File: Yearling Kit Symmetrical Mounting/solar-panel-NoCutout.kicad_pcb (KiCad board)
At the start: 4 copper layers, 83 x 98 mm, 25 parts, among them J1 CON-5040500591, J2 Conn_01x01, J3 Conn_01x01, J4 Conn_01x01, J5 Conn_01x01, U1 VEML7700, U2 MCP9808_DFN, U3 DRV2605LDGS

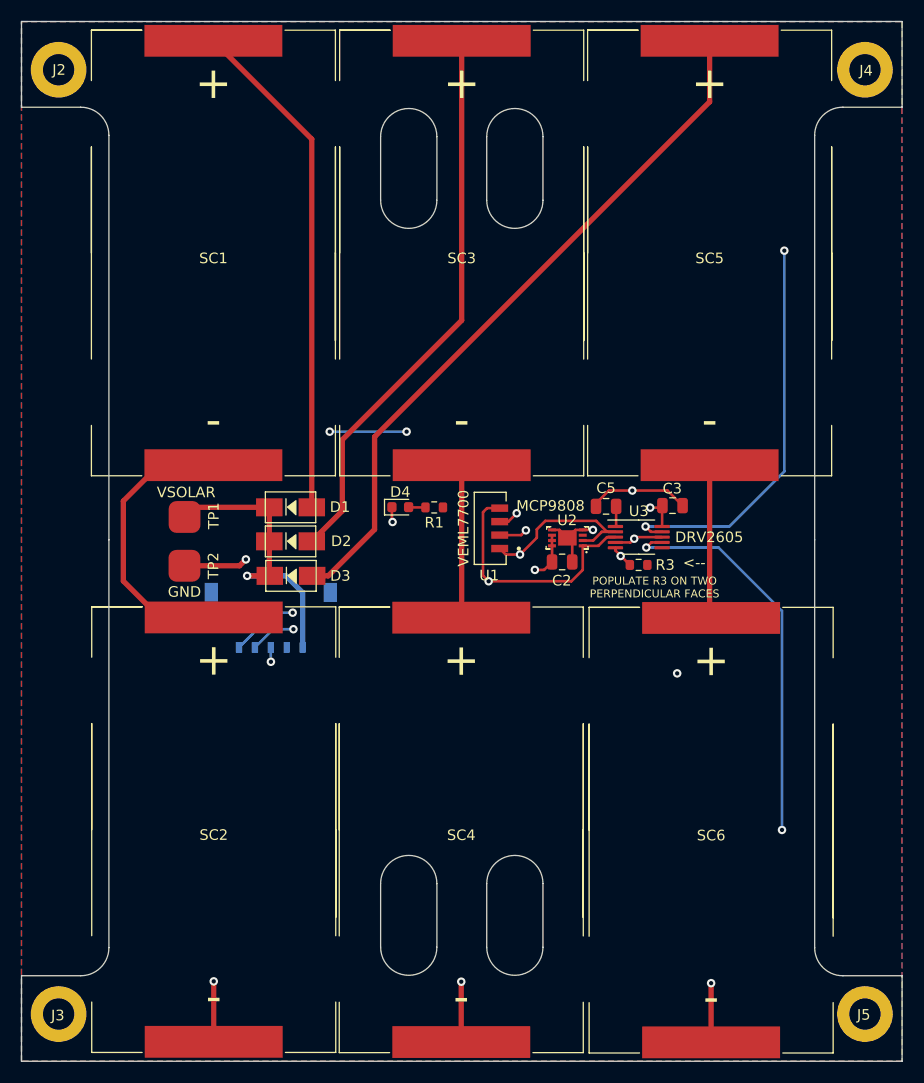
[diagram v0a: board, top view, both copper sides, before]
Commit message: updated no cutout for production
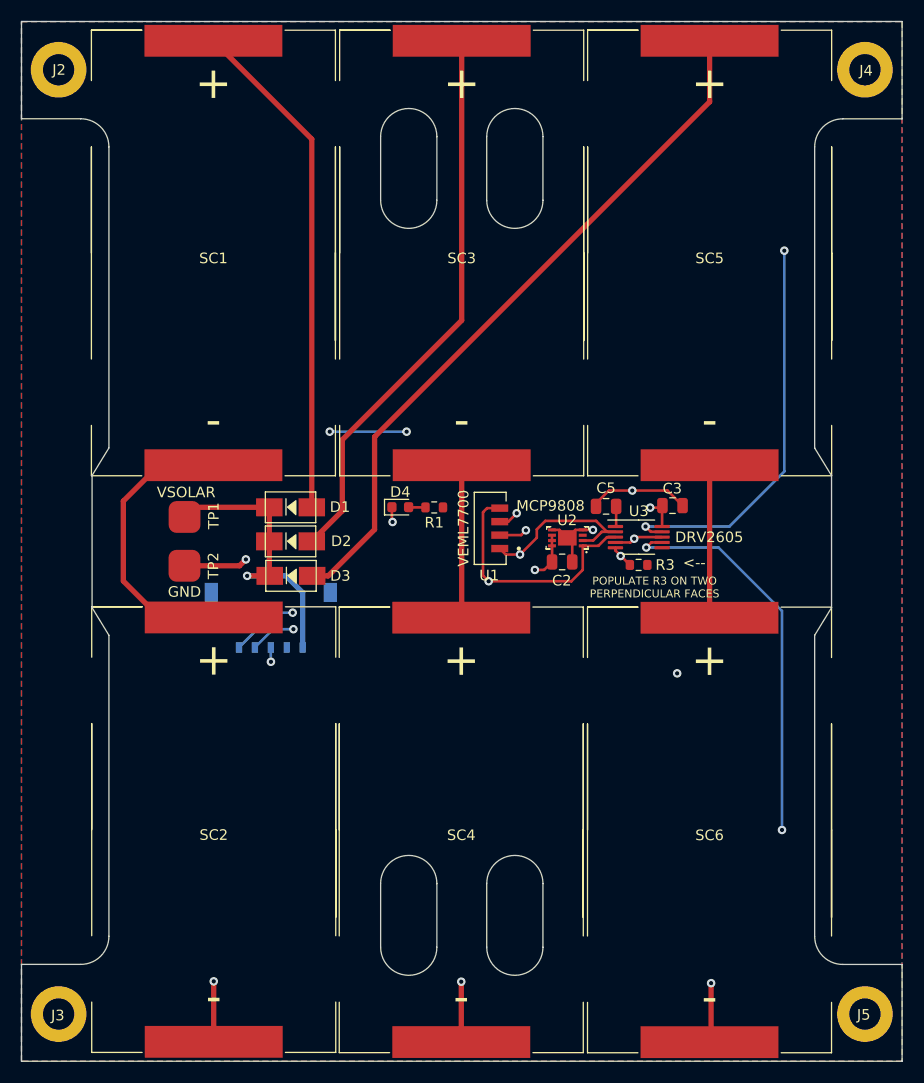
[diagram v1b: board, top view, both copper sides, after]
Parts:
- moved SC6 0.15 mm to (167.8, 141.9)
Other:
- outline, holes or cut-outs redrawn
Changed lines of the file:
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@@
       (rotate (xyz -90 0 0))
+    )
+    (model "C:/Users/bronc/Downloads/solar_cell.step"
+      (offset (xyz -3.4 -0.6 0))
+      (scale (xyz 1 1 1))
+      (rotate (xyz 0 0 0))
     )
   )
@@
       (rotate (xyz -90 0 0))
     )
+    (model "C:/Users/bronc/Downloads/solar_cell.step"
+      (offset (xyz -3.3 -0.6 0))
+      (scale (xyz 1 1 1))
+      (rotate (xyz 0 0 0))
+    )
   )
   (footprint "SolarPanelBoards:KXOB101K08F-TR" (layer "F.Cu")
@@
       (rotate (xyz -90 0 0))
     )
+    (model "C:/Users/bronc/Downloads/solar_cell.step"
+      (offset (xyz -3.3 -0.6 0))
+      (scale (xyz 1 1 1))
+      (rotate (xyz 0 0 0))
+    )
   )
   (footprint "SolarPanelBoards:KXOB101K08F-TR" (layer "F.Cu")
@@
       (rotate (xyz -90 0 0))
     )
+    (model "C:/Users/bronc/Downloads/solar_cell.step"
+      (offset (xyz -3.3 -0.6 0))
+      (scale (xyz 1 1 1))
+      (rotate (xyz 0 0 0))
+    )
   )
   (footprint "SolarPanelBoards:DO-214AC" (layer "F.Cu")
@@
   )
   (footprint "SolarPanelBoards:KXOB101K08F-TR" (layer "F.Cu")
-    (at 168 141.97)
+    (at 167.85 141.95)
     (property "Sheetfile" "solar-panel-NoCutout.kicad_sch")
     (property "Sheetname" "")
@@
       (rotate (xyz -90 0 0))
     )
+    (model "C:/Users/bronc/Downloads/solar_cell.step"
+      (offset (xyz -3.3 -0.6 0))
+      (scale (xyz 1 1 1))
+      (rotate (xyz 0 0 0))
+    )
   )
   (footprint "Capacitor_SMD:C_0805_2012Metric" (layer "F.Cu")
@@
     (pad "4" smd rect locked (at -0.9 1.905 180) (size 1.6 0.7) (layers "F.Cu" "F.Paste" "F.Mask")
       (net 8 "SDA") (pinfunction "SDA") (pintype "bidirectional"))
+    (model "${KIPRJMOD}/Extras/3-DComponents/84592VEML7700.stp"
+      (offset (xyz 0 0 0.3))
+      (scale (xyz 1 1 1))
+      (rotate (xyz 0 0 90))
+    )
   )
   (footprint "Resistor_SMD:R_0603_1608Metric" (layer "F.Cu")
@@
       (scale (xyz 1 1 1))
       (rotate (xyz -90 0 0))
+    )
+    (model "C:/Users/bronc/Downloads/solar_cell.step"
+      (offset (xyz -3.3 -0.6 0))
+      (scale (xyz 1 1 1))
+      (rotate (xyz 0 0 0))
     )
   )
@@
   (gr_line (start 152.15 76.6) (end 152.15 82.6) (layer "Edge.Cuts") (width 0.05))
   (gr_line (start 186 65.75) (end 103 65.75) (layer "Edge.Cuts") (width 0.05))
-  (gr_line (start 108.58 73.83) (end 103 73.83) (layer "Edge.Cuts") (width 0.05))
-  (gr_arc (start 108.58 73.83) (mid 110.461763 74.601155) (end 111.24 76.48) (layer "Edge.Cuts") (width 0.05))
-  (gr_line (start 103 65.75) (end 103 73.83) (layer "Edge.Cuts") (width 0.05))
-  (gr_line (start 103 155.69) (end 103 163.75) (layer "Edge.Cuts") (width 0.05))
+  (gr_line (start 108.58 74.92) (end 103 74.92) (layer "Edge.Cuts") (width 0.05))
+  (gr_arc (start 108.58 74.92) (mid 110.461789 75.69114) (end 111.24 77.57) (layer "Edge.Cuts") (width 0.05))
+  (gr_line (start 103 65.75) (end 103 74.92) (layer "Edge.Cuts") (width 0.05))
+  (gr_line (start 103 154.62) (end 103 163.75) (layer "Edge.Cuts") (width 0.05))
   (gr_arc (start 142.15 82.6) (mid 139.5 85.25) (end 136.85 82.6) (layer "Edge.Cuts") (width 0.05))
-  (gr_line (start 186 73.83) (end 180.42 73.83) (layer "Edge.Cuts") (width 0.05))
-  (gr_line (start 177.76 76.48) (end 177.76 114.6) (layer "Edge.Cuts") (width 0.05))
+  (gr_line (start 186 74.925) (end 180.42 74.925) (layer "Edge.Cuts") (width 0.05))
   (gr_arc (start 146.85 76.6) (mid 149.5 73.95) (end 152.15 76.6) (layer "Edge.Cuts") (width 0.05))
-  (gr_line (start 186 73.83) (end 186 65.75) (layer "Edge.Cuts") (width 0.05))
+  (gr_line (start 186 74.925) (end 186 65.75) (layer "Edge.Cuts") (width 0.05))
   (gr_arc (start 136.85 76.6) (mid 139.5 73.95) (end 142.15 76.6) (layer "Edge.Cuts") (width 0.05))
-  (gr_line (start 111.24 153.04) (end 111.24 114.6) (layer "Edge.Cuts") (width 0.05))
+  (gr_line (start 111.24 123.595) (end 111.24 151.97) (layer "Edge.Cuts") (width 0.05))
+  (gr_line (start 109.65 108.545) (end 109.65 120.995) (layer "Edge.Cuts") (width 0.05))
+  (gr_line (start 109.65 120.995) (end 111.24 123.595) (layer "Edge.Cuts") (width 0.05))
   (gr_line (start 103 163.75) (end 186 163.75) (layer "Edge.Cuts") (width 0.05))
-  (gr_line (start 177.76 114.6) (end 177.76 153.04) (layer "Edge.Cuts") (width 0.05))
   (gr_arc (start 136.85 147) (mid 139.5 144.35) (end 142.15 147) (layer "Edge.Cuts") (width 0.05))
-  (gr_line (start 186 163.75) (end 186 155.69) (layer "Edge.Cuts") (width 0.05))
+  (gr_line (start 186 163.75) (end 186 154.625) (layer "Edge.Cuts") (width 0.05))
   (gr_arc (start 142.15 153) (mid 139.5 155.65) (end 136.85 153) (layer "Edge.Cuts") (width 0.05))
-  (gr_arc (start 177.76 76.48) (mid 178.538215 74.601132) (end 180.42 73.83) (layer "Edge.Cuts") (width 0.05))
-  (gr_line (start 111.24 114.6) (end 111.24 76.48) (layer "Edge.Cuts") (width 0.05))
+  (gr_arc (start 177.76 77.575) (mid 178.538203 75.696102) (end 180.42 74.925) (layer "Edge.Cuts") (width 0.05))
+  (gr_line (start 109.65 108.545) (end 111.24 105.945) (layer "Edge.Cuts") (width 0.05))
+  (gr_line (start 177.76 105.95) (end 179.35 108.55) (layer "Edge.Cuts") (width 0.05))
+  (gr_line (start 177.76 77.575) (end 177.76 105.95) (layer "Edge.Cuts") (width 0.05))
   (gr_arc (start 146.85 147) (mid 149.5 144.35) (end 152.15 147) (layer "Edge.Cuts") (width 0.05))
-  (gr_arc (start 111.24 153.04) (mid 110.461762 154.918833) (end 108.58 155.69) (layer "Edge.Cuts") (width 0.05))
+  (gr_arc (start 111.24 151.97) (mid 110.461768 153.848869) (end 108.58 154.62) (layer "Edge.Cuts") (width 0.05))
+  (gr_line (start 179.35 108.55) (end 179.35 121) (layer "Edge.Cuts") (width 0.05))
   (gr_arc (start 152.15 153) (mid 149.5 155.65) (end 146.85 153) (layer "Edge.Cuts") (width 0.05))
-  (gr_arc (start 180.42 155.69) (mid 178.538244 154.918838) (end 177.76 153.04) (layer "Edge.Cuts") (width 0.05))
-  (gr_line (start 103 155.69) (end 108.58 155.69) (layer "Edge.Cuts") (width 0.05))
+  (gr_line (start 111.24 77.57) (end 111.24 105.945) (layer "Edge.Cuts") (width 0.05))
+  (gr_arc (start 180.42 154.625) (mid 178.538276 153.853824) (end 177.76 151.975) (layer "Edge.Cuts") (width 0.05))
+  (gr_line (start 103 154.62) (end 108.58 154.62) (layer "Edge.Cuts") (width 0.05))
   (gr_arc (start 152.15 82.6) (mid 149.5 85.25) (end 146.85 82.6) (layer "Edge.Cuts") (width 0.05))
-  (gr_line (start 180.42 155.69) (end 186 155.69) (layer "Edge.Cuts") (width 0.05))
+  (gr_line (start 177.76 123.6) (end 177.76 151.975) (layer "Edge.Cuts") (width 0.05))
+  (gr_line (start 177.76 123.6) (end 179.35 121) (layer "Edge.Cuts") (width 0.05))
+  (gr_line (start 180.42 154.625) (end 186 154.625) (layer "Edge.Cuts") (width 0.05))
   (gr_text "VSOLAR" (at 129.39 115.56 270) (layer "B.SilkS")
     (effects (font (size 1 1) (thickness 0.15)) (justify mirror))
